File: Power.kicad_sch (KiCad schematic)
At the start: 33 parts, among them J3 Conn_01x02, U2 TPS56121, U3 LD1117S33TR_SOT223

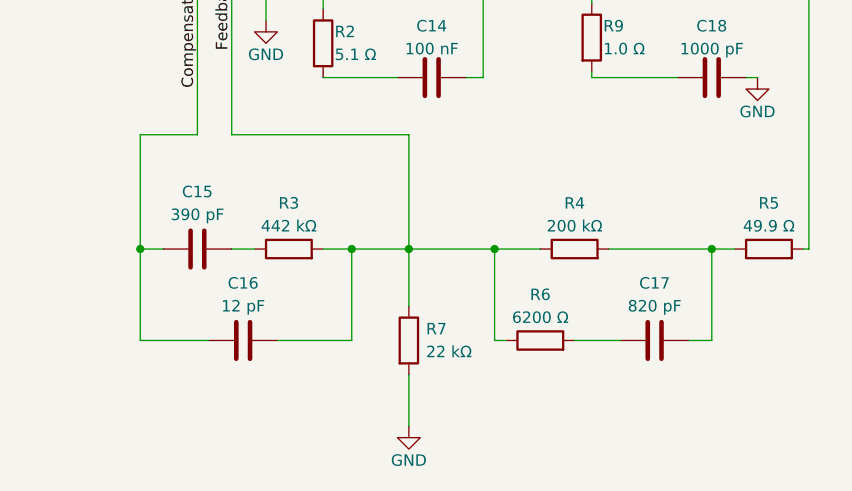
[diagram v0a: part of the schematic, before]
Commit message: Clean up schematic and board layout
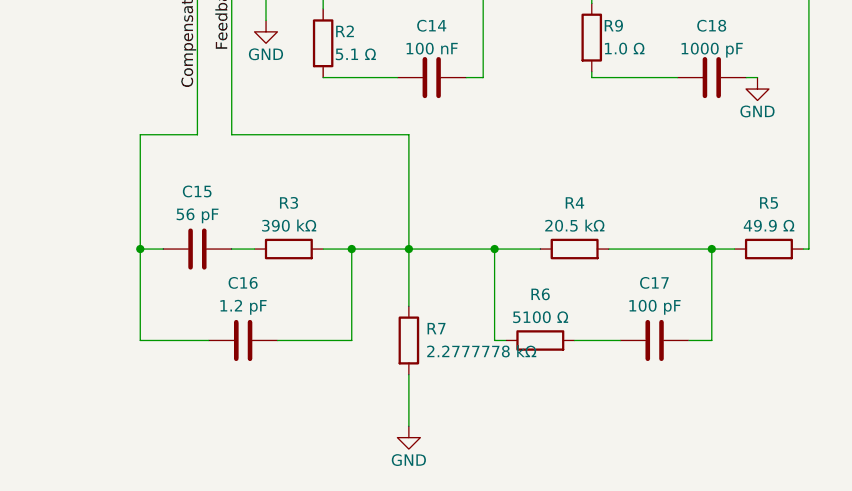
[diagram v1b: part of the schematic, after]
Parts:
- C14: Notes Min 10V rating -> (none)
- C15: value 390 pF -> 56 pF; Part No. CC0805KRX7R9BB391 -> GRM21A5C2E560JW01D
- C16: value 12 pF -> 1.2 pF; Part No. GRM21A5C2D120JW01D -> CC0805BRNPO9BN1R2
- C17: value 820 pF -> 100 pF; Part No. GRM21A5C2E821JWA1J -> CL21C101JCANNNC
- R3: value 442 kΩ -> 390 kΩ; Part No. RC0805FR-07442KL -> RC0805FR-07390KL
- R4: value 200 kΩ -> 20.5 kΩ
- R6: value 6200 Ω -> 5100 Ω; Part No. RC0805FR-076K2L -> RC0805FR-075K1L
- R7: value 22 kΩ -> 2.2777778 kΩ
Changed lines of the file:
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@@
+      (effects (font (size 1.27 1.27)) hide)
+    )
+    (property "Notes" "" (at 174.625 81.28 0)
       (effects (font (size 1.27 1.27)) hide)
     )
@@
     )
     (property "Part No." "GRM32ER71E226KE15K" (at 201.295 81.28 0)
+      (effects (font (size 1.27 1.27)) hide)
+    )
+    (property "Notes" "" (at 201.295 81.28 0)
       (effects (font (size 1.27 1.27)) hide)
     )
@@
       (effects (font (size 1.27 1.27)))
     )
-    (property "Value" "12 pF" (at 64.77 149.86 90)
+    (property "Value" "1.2 pF" (at 64.77 149.86 90)
       (effects (font (size 1.27 1.27)))
     )
@@
       (effects (font (size 1.27 1.27)) hide)
     )
-    (property "Part No." "GRM21A5C2D120JW01D" (at 64.77 153.67 0)
+    (property "Part No." "CC0805BRNPO9BN1R2" (at 64.77 153.67 0)
+      (effects (font (size 1.27 1.27)) hide)
+    )
+    (property "Notes" "" (at 64.77 153.67 0)
       (effects (font (size 1.27 1.27)) hide)
     )
@@
     )
     (property "Part No." "GCM219R72A333KA37D" (at 35.56 90.805 0)
+      (effects (font (size 1.27 1.27)) hide)
+    )
+    (property "Notes" "" (at 35.56 90.805 0)
       (effects (font (size 1.27 1.27)) hide)
     )
@@
       (effects (font (size 1.27 1.27)) hide)
     )
+    (property "Notes" "" (at 187.96 106.045 0)
+      (effects (font (size 1.27 1.27)) hide)
+    )
     (pin "1")
     (pin "2")
@@
       (effects (font (size 1.27 1.27)))
     )
-    (property "Value" "442 kΩ" (at 69.85 140.97 90)
+    (property "Value" "390 kΩ" (at 69.85 140.97 90)
       (effects (font (size 1.27 1.27)))
     )
@@
       (effects (font (size 1.27 1.27)) hide)
     )
-    (property "Part No." "RC0805FR-07442KL" (at 69.85 143.51 0)
+    (property "Part No." "RC0805FR-07390KL" (at 69.85 143.51 0)
       (effects (font (size 1.27 1.27)) hide)
     )
@@
       (effects (font (size 1.27 1.27)))
     )
-    (property "Value" "820 pF" (at 110.49 149.86 90)
+    (property "Value" "100 pF" (at 110.49 149.86 90)
       (effects (font (size 1.27 1.27)))
     )
@@
       (effects (font (size 1.27 1.27)) hide)
     )
-    (property "Part No." "GRM21A5C2E821JWA1J" (at 110.49 153.67 0)
+    (property "Part No." "CL21C101JCANNNC" (at 110.49 153.67 0)
+      (effects (font (size 1.27 1.27)) hide)
+    )
+    (property "Notes" "" (at 110.49 153.67 0)
       (effects (font (size 1.27 1.27)) hide)
     )
@@
       (effects (font (size 1.27 1.27)) hide)
     )
+    (property "Notes" "" (at 90.17 33.02 0)
+      (effects (font (size 1.27 1.27)) hide)
+    )
     (pin "1")
     (pin "2")
@@
       (effects (font (size 1.27 1.27)) hide)
     )
+    (property "Notes" "" (at 174.625 106.045 0)
+      (effects (font (size 1.27 1.27)) hide)
+    )
     (pin "1")
     (pin "2")
@@
       (effects (font (size 1.27 1.27)))
     )
-    (property "Value" "390 pF" (at 59.69 139.7 90)
+    (property "Value" "56 pF" (at 59.69 139.7 90)
       (effects (font (size 1.27 1.27)))
     )
@@
       (effects (font (size 1.27 1.27)) hide)
     )
-    (property "Part No." "CC0805KRX7R9BB391" (at 59.69 143.51 0)
+    (property "Part No." "GRM21A5C2E560JW01D" (at 59.69 143.51 0)
+      (effects (font (size 1.27 1.27)) hide)
+    )
+    (property "Notes" "" (at 59.69 143.51 0)
       (effects (font (size 1.27 1.27)) hide)
     )
@@
       (effects (font (size 1.27 1.27)) (justify left))
     )
-    (property "Value" "22 kΩ" (at 85.09 154.94 0)
+    (property "Value" "2.2777778 kΩ" (at 85.09 154.94 0)
       (effects (font (size 1.27 1.27)) (justify left))
     )
@@
     )
     (property "Part No." "GRM219R7YA105MA12D" (at 161.29 81.28 0)
+      (effects (font (size 1.27 1.27)) hide)
+    )
+    (property "Notes" "" (at 161.29 81.28 0)
       (effects (font (size 1.27 1.27)) hide)
     )
@@
       (effects (font (size 1.27 1.27)) hide)
     )
+    (property "Notes" "" (at 201.295 106.045 0)
+      (effects (font (size 1.27 1.27)) hide)
+    )
     (pin "1")
     (pin "2")
@@
       (effects (font (size 1.27 1.27)))
     )
-    (property "Value" "6200 Ω" (at 97.79 151.13 90)
+    (property "Value" "5100 Ω" (at 97.79 151.13 90)
       (effects (font (size 1.27 1.27)))
     )
@@
       (effects (font (size 1.27 1.27)) hide)
     )
-    (property "Part No." "RC0805FR-076K2L" (at 97.79 153.67 0)
+    (property "Part No." "RC0805FR-075K1L" (at 97.79 153.67 0)
       (effects (font (size 1.27 1.27)) hide)
     )
@@
       (effects (font (size 1.27 1.27)) hide)
     )
+    (property "Notes" "" (at 214.63 106.045 0)
+      (effects (font (size 1.27 1.27)) hide)
+    )
     (pin "1")
     (pin "2")
@@
       (effects (font (size 1.27 1.27)) hide)
     )
+    (property "Notes" "" (at 67.31 66.675 0)
+      (effects (font (size 1.27 1.27)) hide)
+    )
     (pin "1")
     (pin "2")
@@
       (effects (font (size 1.27 1.27)) hide)
     )
+    (property "Notes" "" (at 161.29 106.045 0)
+      (effects (font (size 1.27 1.27)) hide)
+    )
     (pin "1")
     (pin "2")
@@
       (effects (font (size 1.27 1.27)))
     )
-    (property "Value" "200 kΩ" (at 101.6 140.97 90)
+    (property "Value" "20.5 kΩ" (at 101.6 140.97 90)
       (effects (font (size 1.27 1.27)))
     )
@@
       (effects (font (size 1.27 1.27)) hide)
     )
+    (property "Notes" "" (at 214.63 81.28 0)
+      (effects (font (size 1.27 1.27)) hide)
+    )
     (pin "1")
     (pin "2")
@@
       (effects (font (size 1.27 1.27)) hide)
     )
+    (property "Notes" "" (at 187.96 81.28 0)
+      (effects (font (size 1.27 1.27)) hide)
+    )
     (pin "1")
     (pin "2")
@@
       (effects (font (size 1.27 1.27)) hide)
     )
+    (property "Notes" "" (at 116.84 124.46 0)
+      (effects (font (size 1.27 1.27)) hide)
+    )
     (pin "1")
     (pin "2")
@@
       (effects (font (size 1.27 1.27)) hide)
     )
-    (property "Notes" "Min 10V rating" (at 85.725 124.46 90)
+    (property "Notes" "" (at 85.725 124.46 90)
       (effects (font (size 1.27 1.27)) hide)
     )
@@
       (effects (font (size 1.27 1.27)) hide)
     )
+    (property "Notes" "" (at 80.01 66.675 0)
+      (effects (font (size 1.27 1.27)) hide)
+    )

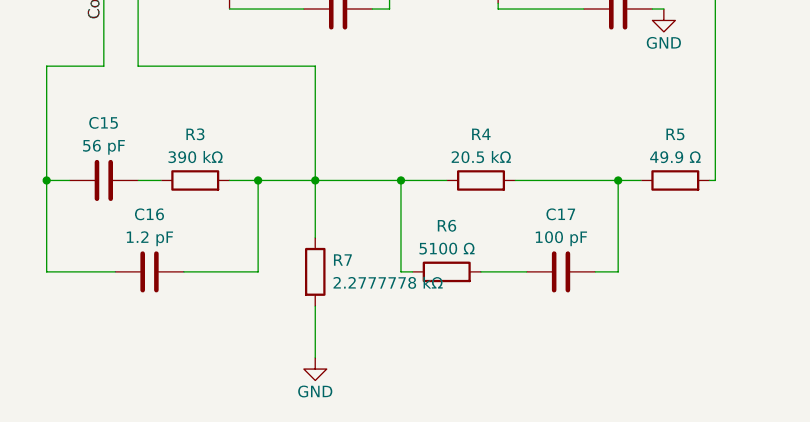
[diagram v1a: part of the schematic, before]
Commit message: Update buck converter voltage divider values and part numbers
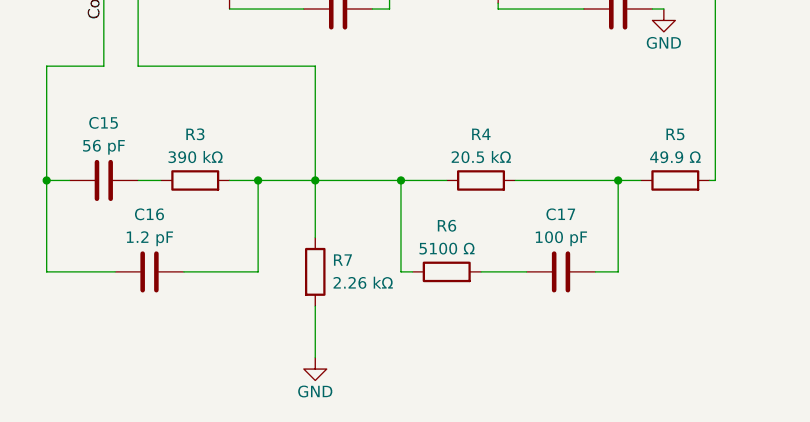
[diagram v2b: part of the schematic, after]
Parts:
- R4: Part No. RC0805FR-07200KL -> RC0805FR-0720K5L
- R7: value 2.2777778 kΩ -> 2.26 kΩ; Part No. RC0805FR-0722KL -> RC0805FR-072K26L
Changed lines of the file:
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@@
       (effects (font (size 1.27 1.27)) (justify left))
     )
-    (property "Value" "2.2777778 kΩ" (at 85.09 154.94 0)
+    (property "Value" "2.26 kΩ" (at 85.09 154.94 0)
       (effects (font (size 1.27 1.27)) (justify left))
     )
@@
       (effects (font (size 1.27 1.27)) hide)
     )
-    (property "Part No." "RC0805FR-0722KL" (at 83.185 153.67 0)
+    (property "Part No." "RC0805FR-072K26L" (at 83.185 153.67 0)
       (effects (font (size 1.27 1.27)) hide)
     )
@@
       (effects (font (size 1.27 1.27)) hide)
     )
-    (property "Part No." "RC0805FR-07200KL" (at 101.6 143.51 0)
-      (effects (font (size 1.27 1.27)) hide)
-    )
+    (property "Part No." "RC0805FR-0720K5L" (at 101.6 143.51 0)
+      (effects (font (size 1.27 1.27)) hide)
+    )
